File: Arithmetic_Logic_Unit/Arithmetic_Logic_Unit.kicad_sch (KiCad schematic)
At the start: 1 part, among them J1 PC104

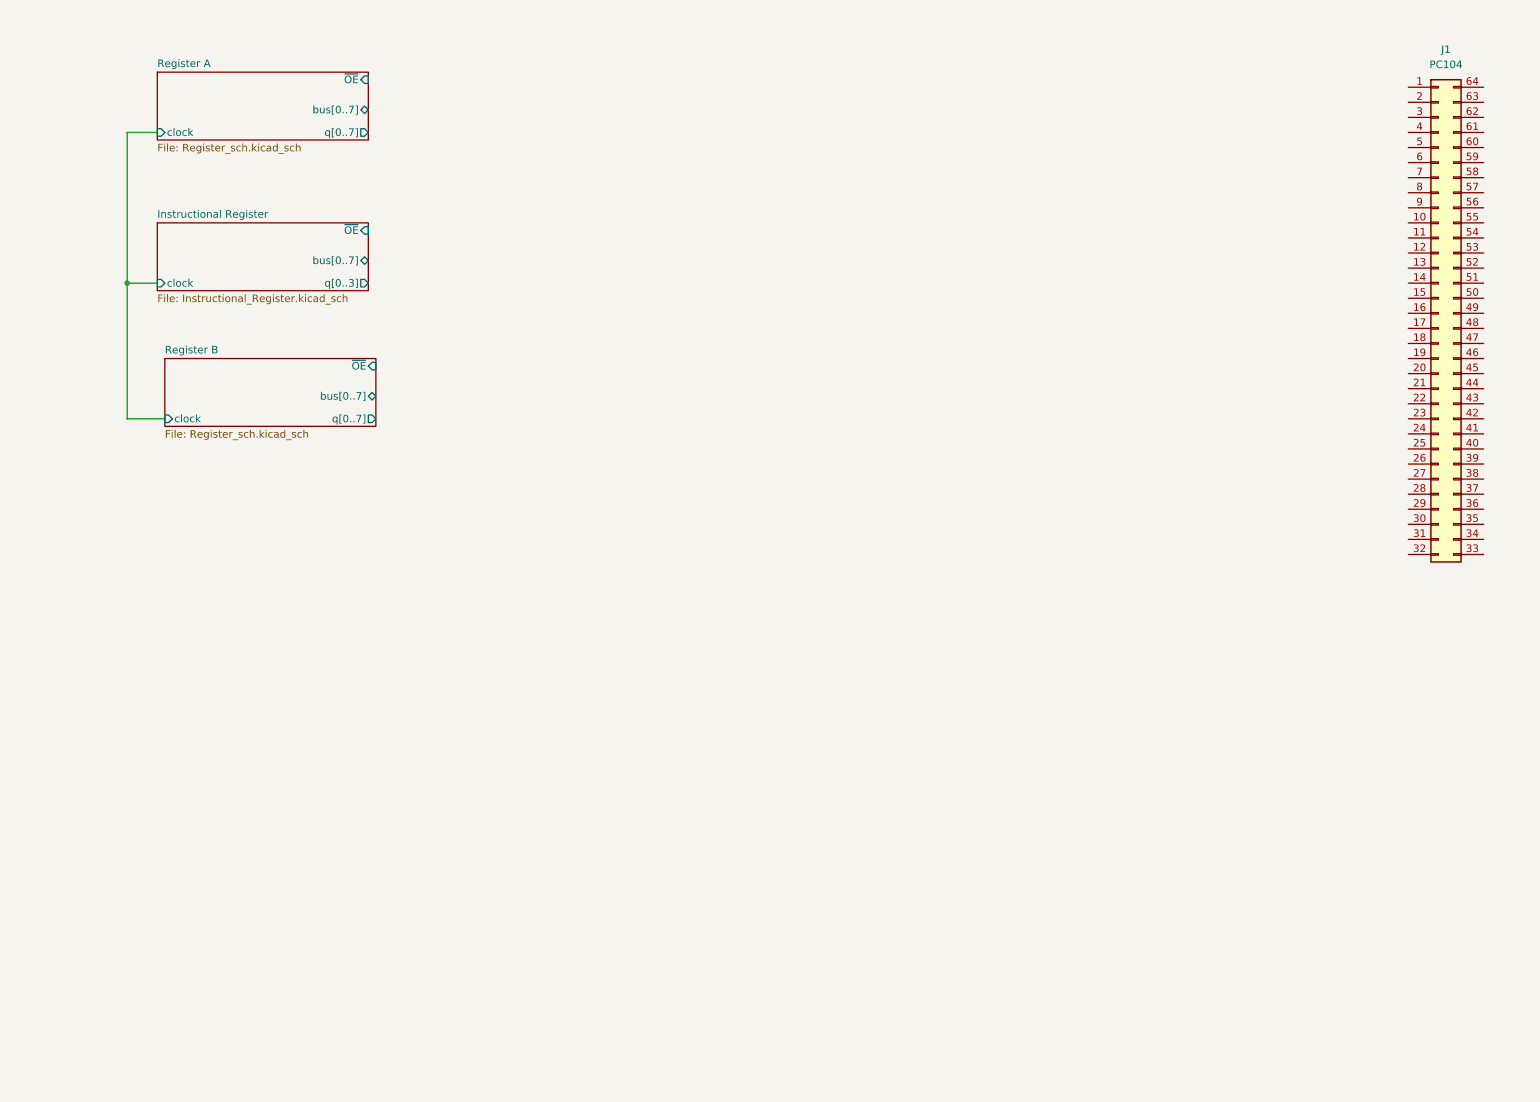
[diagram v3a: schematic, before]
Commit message: completed alu schematic with errors
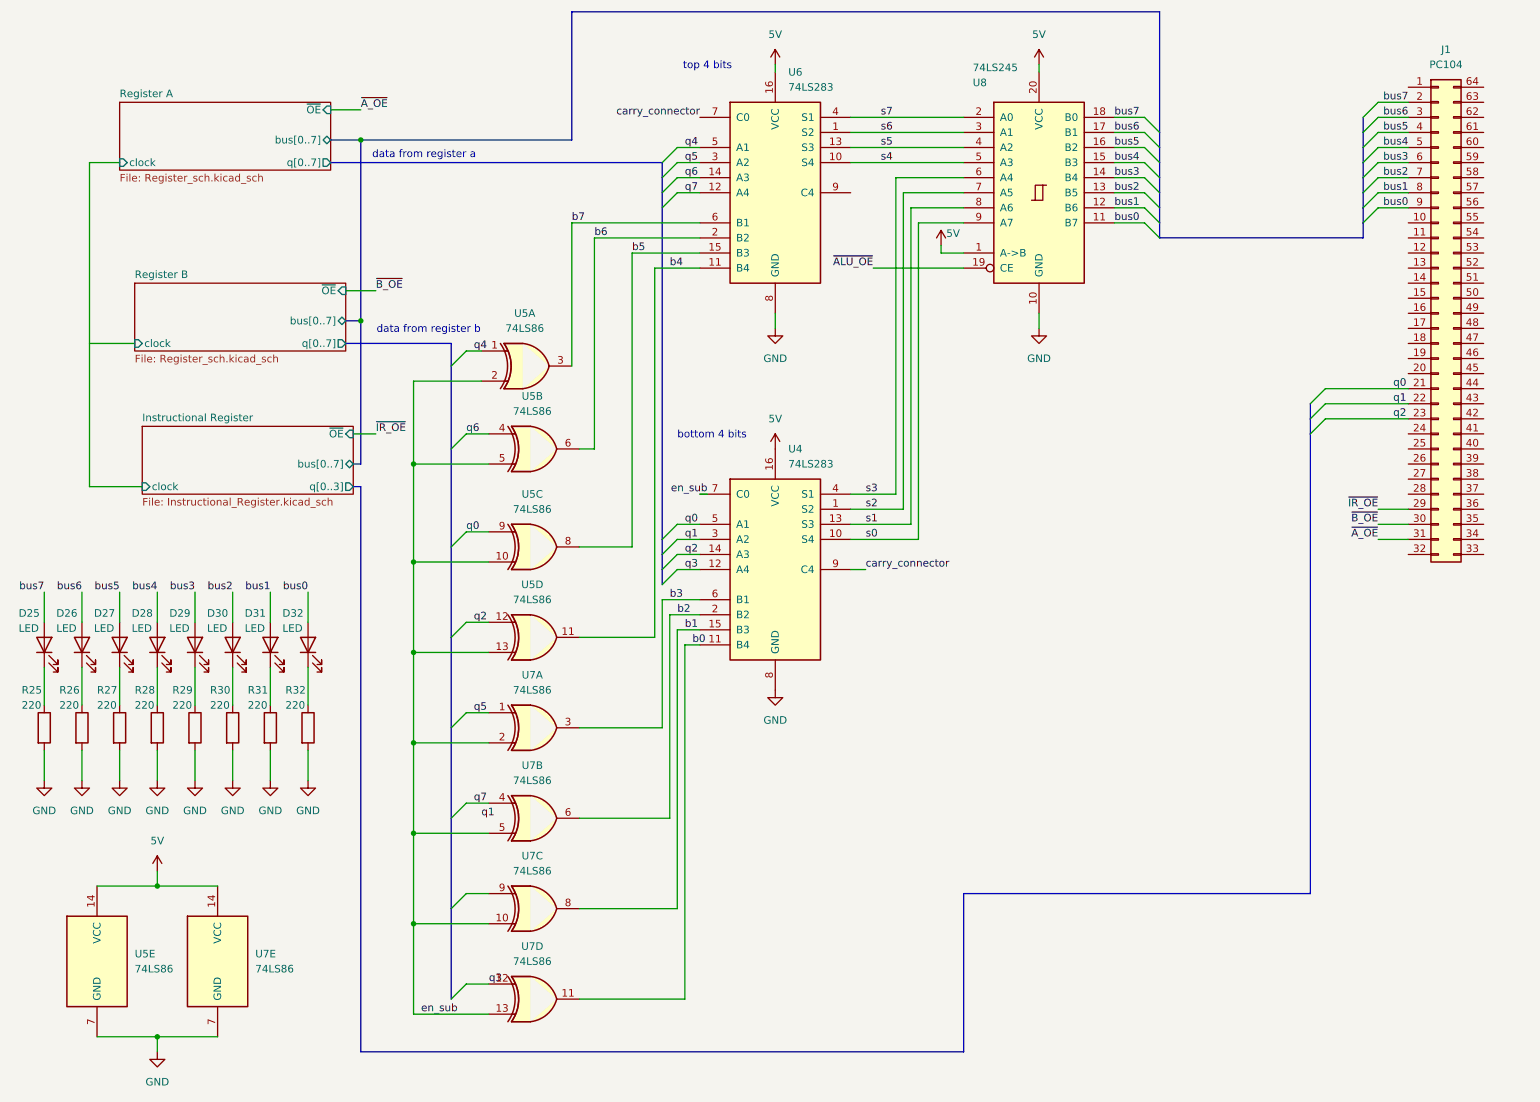
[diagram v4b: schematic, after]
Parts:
- added D25, D26, D27, D28, D29, D30, D31, D32: LED, symbol Device:LED
- added R25, R26, R27, R28, R29, R30, R31, R32: 220, symbol Device:R
- added U4, U6: 74LS283, symbol 74xx:74LS283
- added U5, U7: 74LS86, symbol 74xx:74LS86
- added U8: 74LS245, symbol 74xx:74LS245
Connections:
- net bus7: now reaches J1.2 (Pin_2)
- net bus7: now also D25.2 (A), U8.18 (B0)
- net q0: now reaches J1.21 (Pin_21)
- net q0: now also U4.5 (A1), U5.9
- net q1: now reaches J1.22 (Pin_22)
- net q1: now also U4.3 (A2)
- net q2: now reaches J1.23 (Pin_23)
- net q2: now also U4.14 (A3), U5.12
- net ~{IR_OE}: now reaches J1.29 (Pin_29)
- net bus6: now reaches J1.3 (Pin_3)
- net bus6: now also D26.2 (A), U8.17 (B1)
- net ~{B_OE}: now reaches J1.30 (Pin_30)
- net ~{A_OE}: now reaches J1.31 (Pin_31)
- net bus5: now reaches J1.4 (Pin_4)
- net bus5: now also D27.2 (A), U8.16 (B2)
- net bus4: now reaches J1.5 (Pin_5)
- net bus4: now also D28.2 (A), U8.15 (B3)
- net bus3: now reaches J1.6 (Pin_6)
- net bus3: now also D29.2 (A), U8.14 (B4)
- net bus2: now reaches J1.7 (Pin_7)
- net bus2: now also D30.2 (A), U8.13 (B5)
- net bus1: now reaches J1.8 (Pin_8)
- net bus1: now also D31.2 (A), U8.12 (B6)
- net bus0: now reaches J1.9 (Pin_9)
- net bus0: now also D32.2 (A), U8.11 (B7)
- new net: D25.1 (K), R25.1
- new net: D26.1 (K), R26.1
- new net: D30.1 (K), R30.1
- new net: D28.1 (K), R28.1
- new net: D32.1 (K), R32.1
- new net: D27.1 (K), R27.1
- new net: D29.1 (K), R29.1
- new net: D31.1 (K), R31.1
- new net 5V: U4.16 (VCC), U5.14 (VCC), U6.16 (VCC), U7.14 (VCC), U8.1 (A->B), U8.20 (VCC)
- new net GND: R25.2, R26.2, R27.2, R28.2, R29.2, R30.2, R31.2, R32.2, U4.8 (GND), U5.7 (GND), U6.8 (GND), U7.7 (GND), U8.10 (GND)
- new net b0: U4.11 (B4), U7.11
- new net b1: U4.15 (B3), U7.8
- new net b2: U4.2 (B2), U7.6
- new net b3: U4.6 (B1), U7.3
- new net b4: U5.11, U6.11 (B4)
- new net b5: U5.8, U6.15 (B3)
- new net b6: U5.6, U6.2 (B2)
- new net b7: U5.3, U6.6 (B1)
- new net carry_connector: U4.9 (C4), U6.7 (C0)
- new net en_sub: U4.7 (C0), U5.10, U5.13, U5.2, U5.5, U7.10, U7.13, U7.2, U7.5
- new net q3: U4.12 (A4), U7.12
- new net q4: U5.1, U6.5 (A1)
- new net q5: U6.3 (A2), U7.1
- new net q6: U5.4, U6.14 (A3)
- new net q7: U6.12 (A4), U7.4
- new net s0: U4.10 (S4), U8.9 (A7)
- new net s1: U4.13 (S3), U8.8 (A6)
- new net s2: U4.1 (S2), U8.7 (A5)
- new net s3: U4.4 (S1), U8.6 (A4)
- new net s4: U6.10 (S4), U8.5 (A3)
- new net s5: U6.13 (S3), U8.4 (A2)
- new net s6: U6.1 (S2), U8.3 (A1)
- new net s7: U6.4 (S1), U8.2 (A0)
- new net ~{ALU_OE}: U8.19 (CE)
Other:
- note added: "bottom 4 bits"
- note added: "data from register a"
- note added: "data from register b"
- note added: "top 4 bits"

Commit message: removed buses and replaced with hierarchical labels
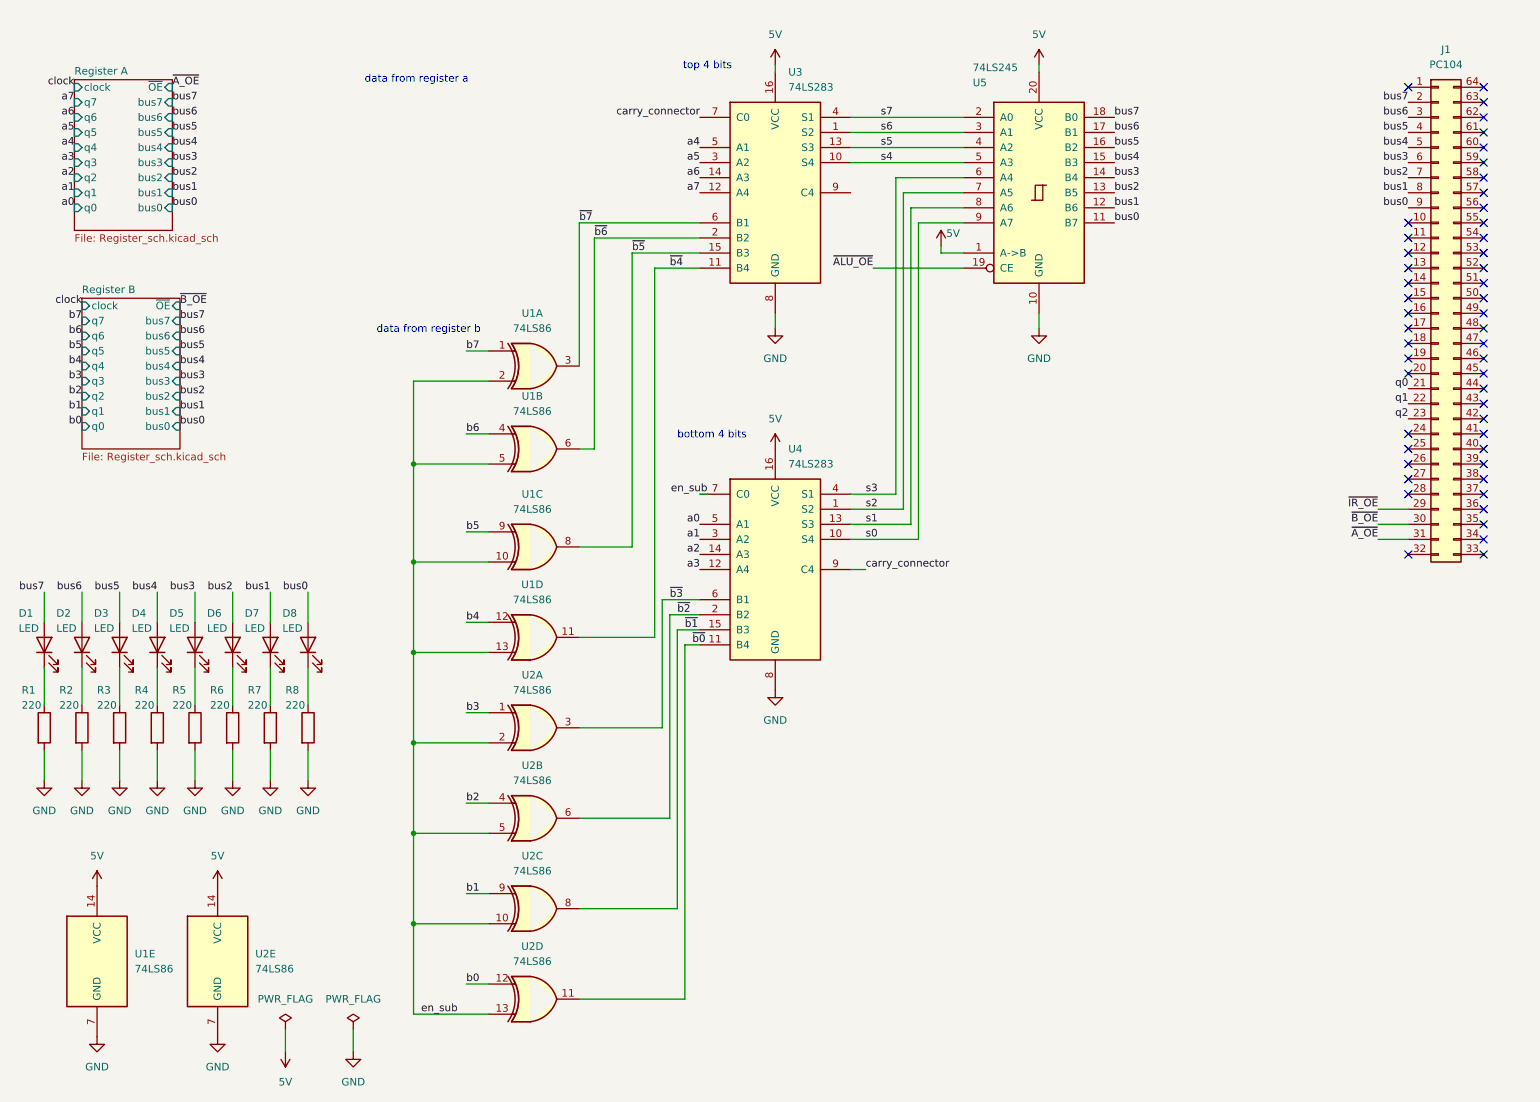
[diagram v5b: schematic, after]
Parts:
- renumbered D25 to D1, D26 to D2, D27 to D3, D28 to D4, D29 to D5, D30 to D6, D31 to D7, D32 to D8, R25 to R1, R26 to R2, R27 to R3, R28 to R4, R29 to R5, R30 to R6, R31 to R7, R32 to R8, U5 to U1, U7 to U2, U6 to U3, U8 to U5
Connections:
- net b0: now also U2.12; no longer U2.11, U4.11 (B4)
- net b1: now also U2.9; no longer U2.8, U4.15 (B3)
- net b2: now also U2.4; no longer U2.6, U4.2 (B2)
- net b3: now also U2.1; no longer U2.3, U4.6 (B1)
- net b4: now also U1.12; no longer U1.11, U3.11 (B4)
- net b5: now also U1.9; no longer U1.8, U3.15 (B3)
- net b6: now also U1.4; no longer U1.6, U3.2 (B2)
- net b7: now also U1.1; no longer U1.3, U3.6 (B1)
- net q0: no longer U1.9, U4.5 (A1)
- net q1: no longer U4.3 (A2)
- net q2: no longer U1.12, U4.14 (A3)
- net q3 renamed a3
- net a3: no longer U2.12
- net q4 renamed a4
- net a4: no longer U1.1
- net q5 renamed a5
- net a5: no longer U2.1
- net q6 renamed a6
- net a6: no longer U1.4
- net q7 renamed a7
- net a7: no longer U2.4
- new net a0: U4.5 (A1)
- new net a1: U4.3 (A2)
- new net a2: U4.14 (A3)
- new net ~{b0}: U2.11, U4.11 (B4)
- new net ~{b1}: U2.8, U4.15 (B3)
- new net ~{b2}: U2.6, U4.2 (B2)
- new net ~{b3}: U2.3, U4.6 (B1)
- new net ~{b4}: U1.11, U3.11 (B4)
- new net ~{b5}: U1.8, U3.15 (B3)
- new net ~{b6}: U1.6, U3.2 (B2)
- new net ~{b7}: U1.3, U3.6 (B1)
- no-connect marks 0 -> 50
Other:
- removed sheet Instructional Register
- sheet Register A ports: added bus0, bus1, bus2, bus3, bus4, bus5, bus6, bus7, q0, q1, q2, q3, q4, q5, q6, q7; removed bus[0..7], q[0..7]
- sheet Register B ports: added bus0, bus1, bus2, bus3, bus4, bus5, bus6, bus7, q0, q1, q2, q3, q4, q5, q6, q7; removed bus[0..7], q[0..7]
- moved on the sheet: U1A

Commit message: added instructional register
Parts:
- removed D1, D2, D3, D4, D5, D6, D7, D8: LED, symbol Device:LED
- removed R1, R2, R3, R4, R5, R6, R7, R8: 220, symbol Device:R
- removed U1, U2: 74LS86, symbol 74xx:74LS86
- removed U3, U4: 74LS283, symbol 74xx:74LS283
- removed U5: 74LS245, symbol 74xx:74LS245
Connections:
- net 5V: now also J1.36 (Pin_36), J1.62 (Pin_62)
- net GND: now also J1.32 (Pin_32), J1.33 (Pin_33), J1.34 (Pin_34), J1.64 (Pin_64)
- net clock: now also J1.45 (Pin_45)
- net en_sub: now also J1.27 (Pin_27)
- net ~{ALU_OE}: now also J1.28 (Pin_28)
- net ir4: now reaches J1.24 (Pin_24)
- net q0 renamed ir7
- net q1 renamed ir6
- net q2 renamed ir5
- no-connect marks 50 -> 40
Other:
- removed sheet Register A
- removed sheet Register B
- added sheet ALU (ALU.kicad_sch)
- added sheet Instruction Register (ir.kicad_sch)
- note removed: "bottom 4 bits"
- note removed: "data from register a"
- note removed: "data from register b"
- note removed: "top 4 bits"

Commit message: added flags
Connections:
- net cf: now reaches J1.17 (Pin_17)
- net zf: now reaches J1.18 (Pin_18)
- net clear: now reaches J1.19 (Pin_19)
- net fi: now reaches J1.20 (Pin_20)
- no-connect marks 40 -> 36
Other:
- sheet ALU ports: added cf, clear, fi, zf; removed none
